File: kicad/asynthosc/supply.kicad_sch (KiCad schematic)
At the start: 52 parts, among them J1 USB_B_Micro, J17 Conn_01x02, J2 Conn_02x05_Odd_Even, U1 LM1117S-3.3, U2 LMR62421XMF, U3 USBLC6-2SC6, U4 LM1117S-5.0, U5 Si1869DH

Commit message: bom: adding jlc ref to generic
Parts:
- C1, C2, C4, C8, C9: LCSC (none) -> C49678
- C10: LCSC (none) -> C15195
- C11, C59: LCSC (none) -> C307331
- C6: LCSC (none) -> C113781
- C7: LCSC (none) -> C16780
- F1: LCSC (none) -> C883114
- R1, R2, R3, R5, R6: LCSC (none) -> C25744
- R4: LCSC (none) -> C304634
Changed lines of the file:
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@@
 			)
 		)
-		(property "LCSC" ""
+		(property "LCSC" "C49678"
 			(at 39.37 92.71 0)
 			(effects
@@
 			)
 		)
-		(property "LCSC" ""
+		(property "LCSC" "C49678"
 			(at 120.65 259.08 0)
 			(effects
@@
 			)
 		)
-		(property "LCSC" ""
+		(property "LCSC" "C25744"
 			(at 29.21 187.96 0)
 			(effects
@@
 			)
 		)
-		(property "LCSC" ""
+		(property "LCSC" "C15195"
 			(at 154.94 46.99 0)
 			(effects
@@
 			)
 		)
-		(property "LCSC" ""
+		(property "LCSC" "C16780"
 			(at 91.44 213.36 0)
 			(effects
@@
 			)
 		)
-		(property "LCSC" ""
+		(property "LCSC" "C25744"
 			(at 29.21 198.12 0)
 			(effects
@@
 			)
 		)
-		(property "LCSC" ""
+		(property "LCSC" "C307331"
 			(at 175.26 46.99 0)
 			(effects
@@
 			)
 		)
-		(property "LCSC" ""
+		(property "LCSC" "C307331"
 			(at 213.36 261.62 0)
 			(effects
@@
 			)
 		)
-		(property "LCSC" ""
+		(property "LCSC" "C49678"
 			(at 40.64 146.05 0)
 			(effects
@@
 			)
 		)
-		(property "LCSC" ""
+		(property "LCSC" "C25744"
 			(at 69.85 210.82 0)
 			(effects
@@
 			)
 		)
-		(property "LCSC" ""
+		(property "LCSC" "C113781"
 			(at 82.55 203.2 0)
 			(effects
@@
 			)
 		)
-		(property "LCSC" ""
+		(property "LCSC" "C49678"
 			(at 91.44 259.08 0)
 			(effects
@@
 			)
 		)
-		(property "LCSC" ""
+		(property "LCSC" "C883114"
 			(at 93.98 38.1 0)
 			(effects
@@
 			)
 		)
-		(property "LCSC" ""
+		(property "LCSC" "C25744"
 			(at 182.88 257.81 0)
 			(effects
@@
 			)
 		)
-		(property "LCSC" ""
+		(property "LCSC" "C25744"
 			(at 176.53 264.16 0)
 			(effects
@@
 			)
 		)
-		(property "LCSC" ""
+		(property "LCSC" "C49678"
 			(at 68.58 92.71 0)
 			(effects
@@
 			)
 		)
-		(property "LCSC" ""
+		(property "LCSC" "C304634"
 			(at 82.55 193.04 0)
 			(effects

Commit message: bom: update jlcpcb part numbers
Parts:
- F1: LCSC C883114 -> C70063
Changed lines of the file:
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@@
 			)
 		)
-		(property "LCSC" "C883114"
+		(property "LCSC" "C70063"
 			(at 93.98 38.1 0)
 			(effects

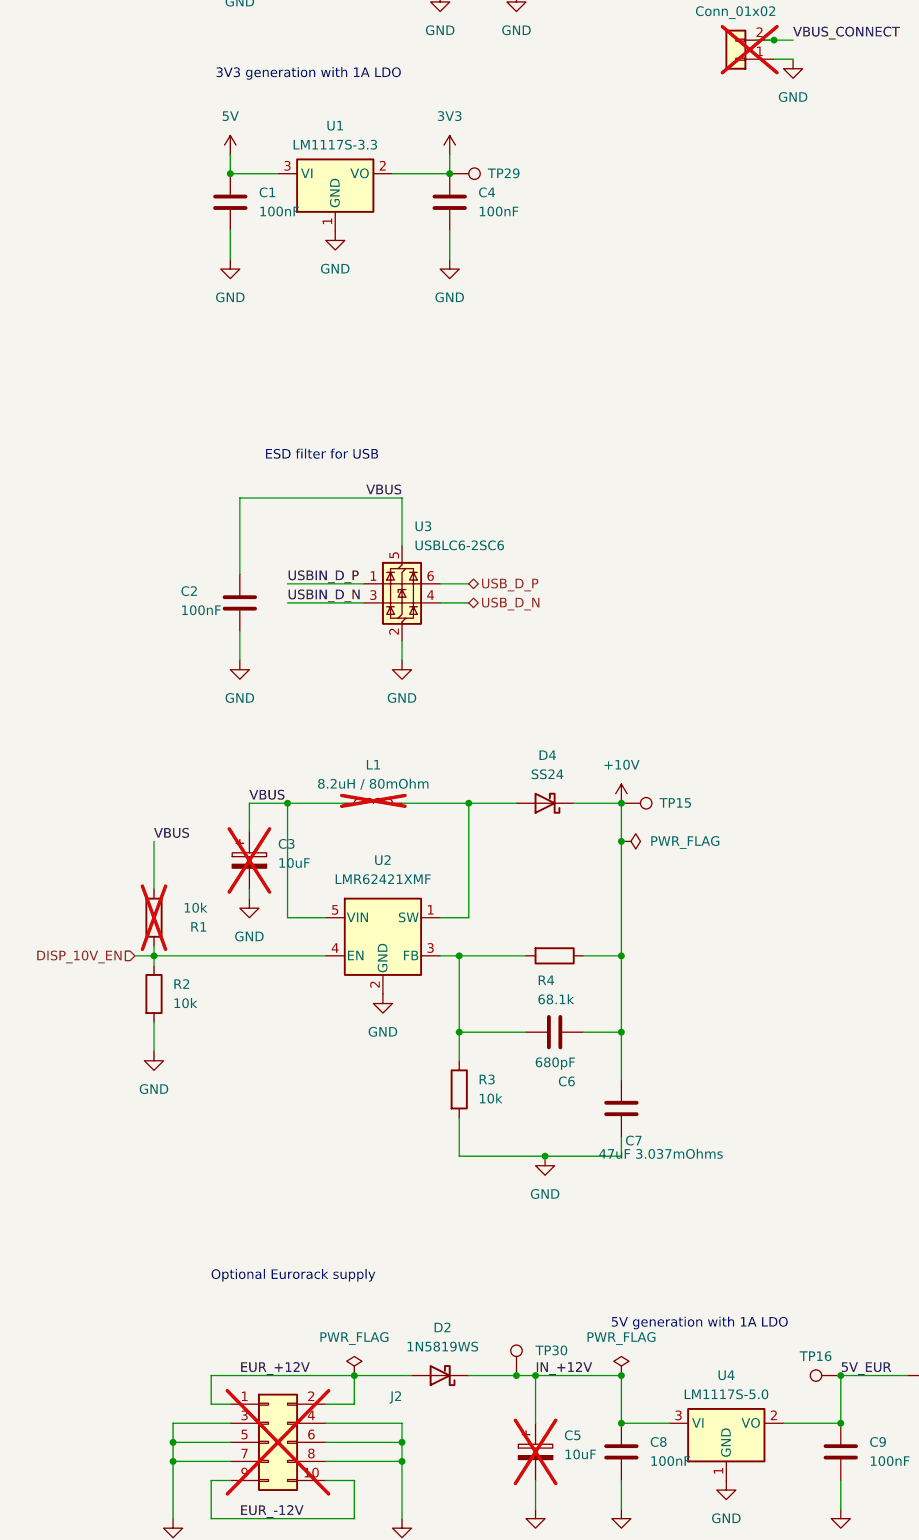
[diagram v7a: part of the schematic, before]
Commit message: sch: bom: fix footprints and bom
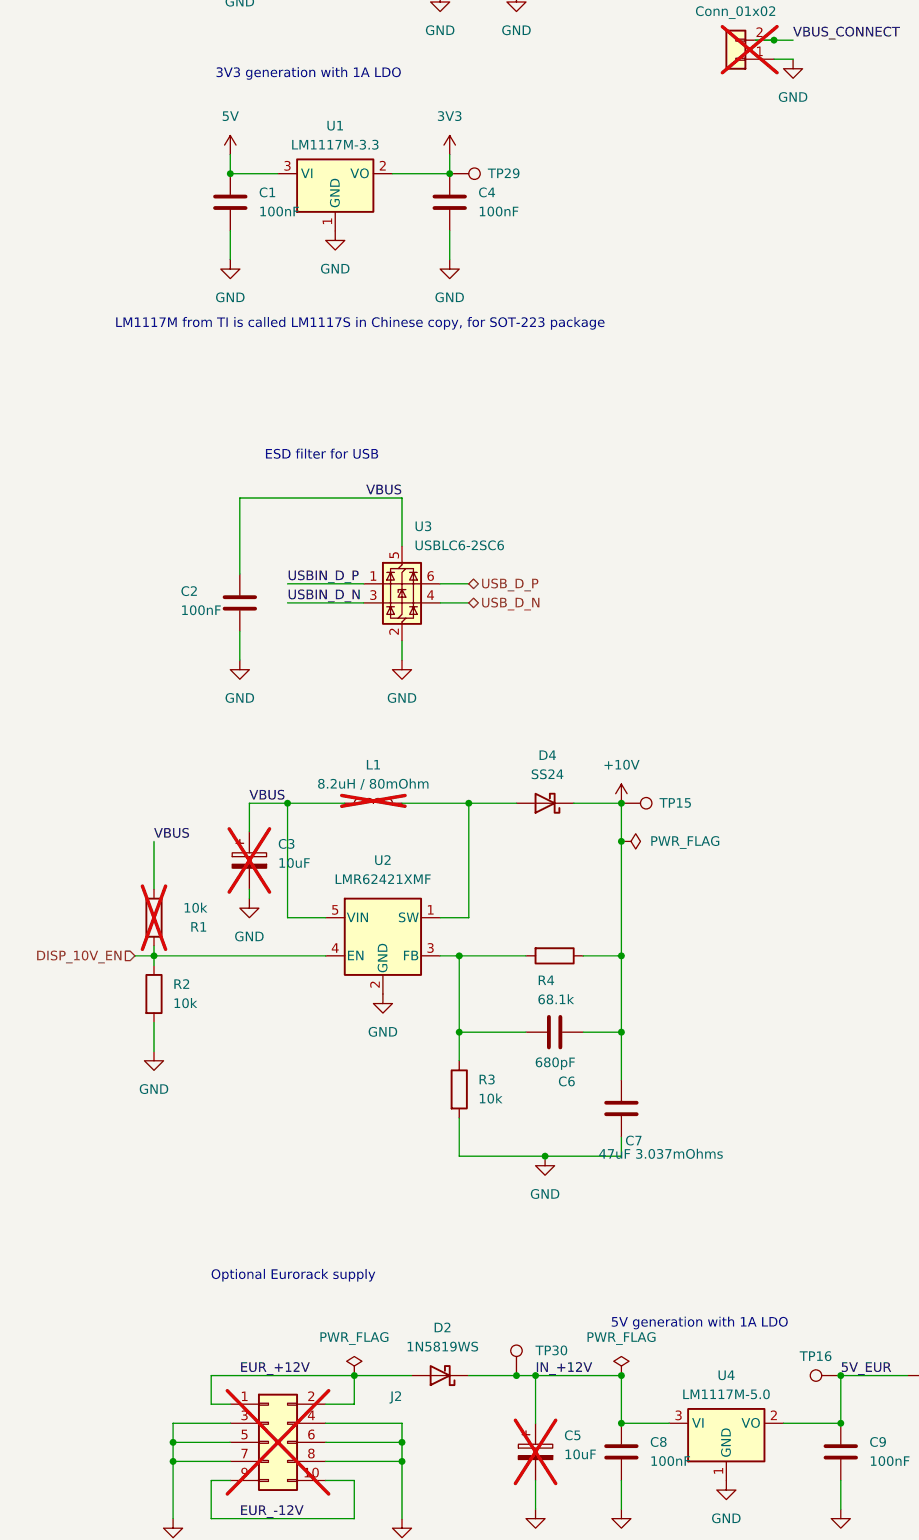
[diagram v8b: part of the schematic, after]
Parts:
- U1: value LM1117S-3.3 -> LM1117M-3.3
- U4: value LM1117S-5.0 -> LM1117M-5.0
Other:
- note added: "LM1117M from TI is called LM1117S in Chinese copy, for SOT-223 package"
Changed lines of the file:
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@@
 		)
 	)
+	(text "LM1117M from TI is called LM1117S in Chinese copy, for SOT-223 package"
+		(exclude_from_sim no)
+		(at 56.642 108.966 0)
+		(effects
+			(font
+				(size 1.27 1.27)
+			)
+		)
+	)
 	(text "Optional Eurorack supply"
 		(exclude_from_sim no)
@@
 			)
 		)
-		(property "Value" "LM1117S-5.0"
+		(property "Value" "LM1117M-5.0"
 			(at 105.41 251.46 0)
 			(effects
@@
 			)
 		)
-		(property "Value" "LM1117S-3.3"
+		(property "Value" "LM1117M-3.3"
 			(at 53.34 85.09 0)
 			(effects
@@
 			)
 		)
-		(property "Datasheet" "https://www.lcsc.com/datasheet/lcsc_datasheet_2307121520_XR-XRCD75-8R2M_C7462918.pdf"
+		(property "Datasheet" "~"
 			(at 58.42 172.72 0)
 			(effects
